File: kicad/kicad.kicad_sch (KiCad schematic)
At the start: 28 parts, among them J101 DEBUG_LED_CONN, J102 EPD_SPI_CONN, J103 HPC_CONN, J104 STORAGE_CONN, J105 MGMT_CONN, J106 GLOBAL_CONN, J107 INPUT_CONN, J109 USBC_CONN

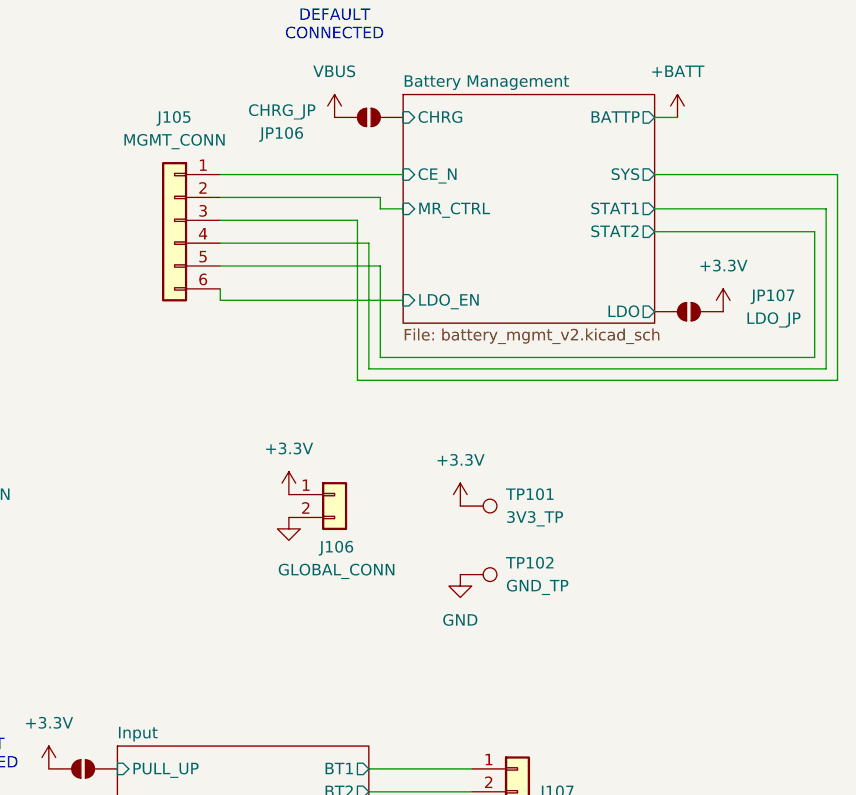
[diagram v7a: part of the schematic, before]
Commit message: slight refactoring, fix LDO power-path
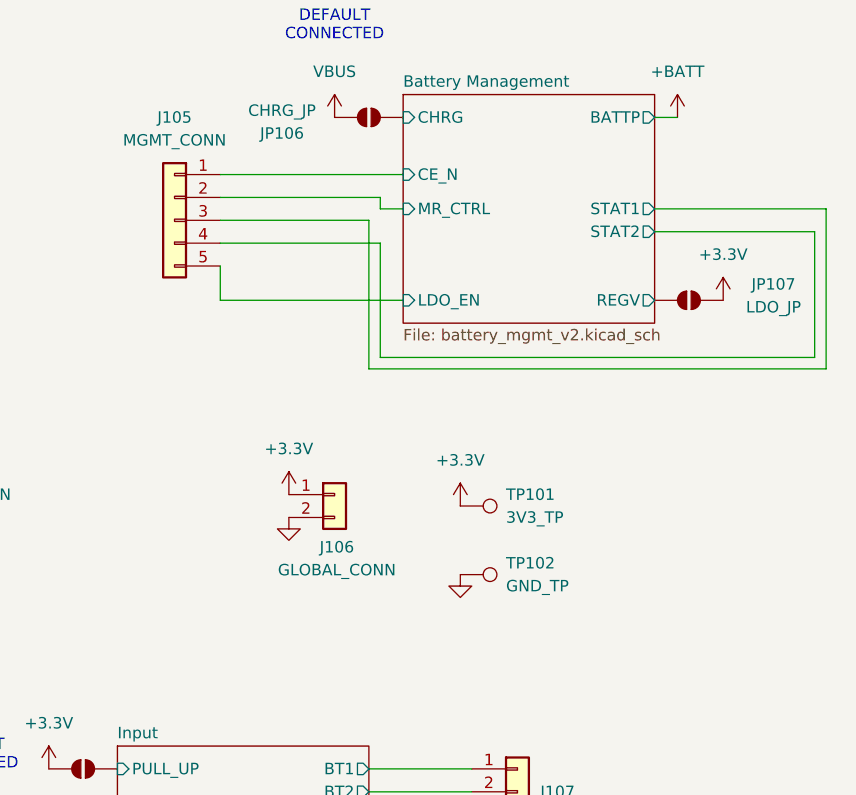
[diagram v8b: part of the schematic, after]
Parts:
- removed J105: MGMT_CONN, Connector_JST:JST_XH_B6B-XH-A_1x06_P2.50mm_Vertical, symbol Connector_Generic:Conn_01x06
- added J105: MGMT_CONN, symbol Connector_Generic:Conn_01x05
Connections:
- net Battery Management/CE_N: now also J105.1 (Pin_1)
- net Battery Management/LDO_EN: now also J105.5 (Pin_5)
- net Battery Management/MR_CTRL: now also J105.2 (Pin_2)
- net Battery Management/STAT1: now also J105.3 (Pin_3)
- net Battery Management/STAT2: now also J105.4 (Pin_4)
- net Battery Management/LDO renamed Battery Management/REGV
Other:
- sheet Battery Management ports: added REGV; removed LDO, SYS
- moved on the sheet: JP107
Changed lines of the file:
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@@
 	(wire
 		(pts
-			(xy 210.82 59.69) (xy 210.82 73.66)
+			(xy 210.82 57.15) (xy 210.82 73.66)
 		)
 		(stroke
@@
 	(wire
 		(pts
-			(xy 194.31 59.69) (xy 210.82 59.69)
+			(xy 210.82 118.11) (xy 222.25 118.11)
 		)
 		(stroke
@@
 	(wire
 		(pts
-			(xy 210.82 118.11) (xy 222.25 118.11)
+			(xy 260.35 72.39) (xy 260.35 58.42)
 		)
 		(stroke
@@
 	(wire
 		(pts
-			(xy 260.35 72.39) (xy 260.35 58.42)
+			(xy 38.1 138.43) (xy 67.31 138.43)
 		)
 		(stroke
@@
 	(wire
 		(pts
-			(xy 38.1 138.43) (xy 67.31 138.43)
+			(xy 194.31 57.15) (xy 210.82 57.15)
 		)
 		(stroke
@@
 	(wire
 		(pts
-			(xy 194.31 66.04) (xy 194.31 64.77)
-		)
-		(stroke
-			(width 0)
-			(type default)
-		)
-	)
-	(wire
-		(pts
-			(xy 209.55 74.93) (xy 262.89 74.93)
+			(xy 148.59 99.06) (xy 148.59 120.65)
 		)
 		(stroke
@@
 	(wire
 		(pts
-			(xy 148.59 99.06) (xy 148.59 120.65)
+			(xy 194.31 59.69) (xy 212.09 59.69)
 		)
 		(stroke
@@
 	(wire
 		(pts
-			(xy 209.55 57.15) (xy 209.55 74.93)
-		)
-		(stroke
-			(width 0)
-			(type default)
-		)
-	)
-	(wire
-		(pts
-			(xy 194.31 62.23) (xy 212.09 62.23)
-		)
-		(stroke
-			(width 0)
-			(type default)
-		)
-	)
-	(wire
-		(pts
 			(xy 151.13 119.38) (xy 151.13 101.6)
 		)
@@
 	(wire
 		(pts
-			(xy 262.89 52.07) (xy 242.57 52.07)
-		)
-		(stroke
-			(width 0)
-			(type default)
-		)
-	)
-	(wire
-		(pts
-			(xy 262.89 74.93) (xy 262.89 52.07)
+			(xy 194.31 52.07) (xy 214.63 52.07)
 		)
 		(stroke
@@
 	(wire
 		(pts
-			(xy 194.31 52.07) (xy 214.63 52.07)
+			(xy 110.49 167.64) (xy 124.46 167.64)
 		)
 		(stroke
@@
 	(wire
 		(pts
-			(xy 110.49 167.64) (xy 124.46 167.64)
+			(xy 210.82 123.19) (xy 222.25 123.19)
 		)
 		(stroke
@@
 	(wire
 		(pts
-			(xy 210.82 123.19) (xy 222.25 123.19)
+			(xy 123.19 162.56) (xy 110.49 162.56)
 		)
 		(stroke
@@
 	(wire
 		(pts
-			(xy 123.19 162.56) (xy 110.49 162.56)
+			(xy 194.31 62.23) (xy 194.31 66.04)
 		)
 		(stroke
@@
 	(wire
 		(pts
-			(xy 212.09 62.23) (xy 212.09 72.39)
-		)
-		(stroke
-			(width 0)
-			(type default)
-		)
-	)
-	(wire
-		(pts
-			(xy 214.63 66.04) (xy 194.31 66.04)
+			(xy 212.09 59.69) (xy 212.09 72.39)
 		)
 		(stroke
@@
 	(wire
 		(pts
-			(xy 194.31 57.15) (xy 209.55 57.15)
+			(xy 261.62 73.66) (xy 261.62 55.88)
 		)
 		(stroke
@@
 	(wire
 		(pts
-			(xy 261.62 73.66) (xy 261.62 55.88)
+			(xy 194.31 66.04) (xy 214.63 66.04)
 		)
 		(stroke
@@
 					(size 1.27 1.27)
 				)
+				(hide yes)
 			)
 		)
@@
 	)
 	(symbol
+		(lib_id "Connector_Generic:Conn_01x05")
+		(at 189.23 57.15 0)
+		(mirror y)
+		(unit 1)
+		(exclude_from_sim no)
+		(in_bom yes)
+		(on_board yes)
+		(dnp no)
+		(fields_autoplaced yes)
+		(property "Reference" "J105"
+			(at 189.23 45.72 0)
+			(effects
+				(font
+					(size 1.27 1.27)
+				)
+			)
+		)
+		(property "Value" "MGMT_CONN"
+			(at 189.23 48.26 0)
+			(effects
+				(font
+					(size 1.27 1.27)
+				)
+			)
+		)
+		(property "Footprint" ""
+			(at 189.23 57.15 0)
+			(effects
+				(font
+					(size 1.27 1.27)
+				)
+				(hide yes)
+			)
+		)
+		(property "Datasheet" "~"
+			(at 189.23 57.15 0)
+			(effects
+				(font
+					(size 1.27 1.27)
+				)
+				(hide yes)
+			)
+		)
+		(property "Description" "Generic connector, single row, 01x05, script generated (kicad-library-utils/schlib/autogen/connector/)"
+			(at 189.23 57.15 0)
+			(effects
+				(font
+					(size 1.27 1.27)
+				)
+				(hide yes)
+			)
+		)
+		(pin "5"
+		)
+		(pin "3"
+		)
+		(pin "1"
+		)
+		(pin "2"
+		)
+		(pin "4"
+		)
+		(instances
+			(project "kicad"
+				(path "/97e37379-fec6-4f0d-82d9-4ea53516bb02"
+					(reference "J105")
+					(unit 1)
+				)
+			)
+		)
+	)
+	(symbol
 		(lib_id "Device:R")
 		(at 63.5 104.14 0)
@@
 	)
 	(symbol
-		(lib_id "Connector_Generic:Conn_01x06")
-		(at 189.23 57.15 0)
-		(mirror y)
-		(unit 1)
-		(exclude_from_sim no)
-		(in_bom yes)
-		(on_board yes)
-		(dnp no)
-		(property "Reference" "J105"
-			(at 189.23 45.72 0)
-			(effects
-				(font
-					(size 1.27 1.27)
-				)
-			)
-		)
-		(property "Value" "MGMT_CONN"
-			(at 189.23 48.26 0)
-			(effects
-				(font
-					(size 1.27 1.27)
-				)
-			)
-		)
-		(property "Footprint" "Connector_JST:JST_XH_B6B-XH-A_1x06_P2.50mm_Vertical"
-			(at 189.23 57.15 0)
-			(effects
-				(font
-					(size 1.27 1.27)
-				)
-				(hide yes)
-			)
-		)
-		(property "Datasheet" "~"
-			(at 189.23 57.15 0)
-			(effects
-				(font
-					(size 1.27 1.27)
-				)
-				(hide yes)
-			)
-		)
-		(property "Description" "Generic connector, single row, 01x06, script generated (kicad-library-utils/schlib/autogen/connector/)"
-			(at 189.23 57.15 0)
-			(effects
-				(font
-					(size 1.27 1.27)
-				)
-				(hide yes)
-			)
-		)
-		(property "JLC" "XXXXXX"
-			(at 189.23 57.15 0)
-			(effects
-				(font
-					(size 1.27 1.27)
-				)
-				(hide yes)
-			)
-		)
-		(property "LCSC" "XXXXXX"
-			(at 189.23 57.15 0)
-			(effects
-				(font
-					(size 1.27 1.27)
-				)
-				(hide yes)
-			)
-		)
-		(pin "5"
-		)
-		(pin "2"
-		)
-		(pin "4"
-		)
-		(pin "6"
-		)
-		(pin "1"
-		)
-		(pin "3"
-		)
-		(instances
-			(project "kicad"
-				(path "/97e37379-fec6-4f0d-82d9-4ea53516bb02"
-					(reference "J105")
-					(unit 1)
-				)
-			)
-		)
-	)
-	(symbol
 		(lib_id "power:VBUS")
 		(at 149.86 45.72 0)
@@
 	(symbol
 		(lib_id "power:+3.3V")
-		(at 250.19 67.31 0)
+		(at 250.19 66.04 0)
 		(unit 1)
 		(exclude_from_sim no)
@@
 		(fields_autoplaced yes)
 		(property "Reference" "#PWR0122"
-			(at 250.19 71.12 0)
+			(at 250.19 69.85 0)
 			(effects
 				(font
@@
 		)
 		(property "Value" "+3.3V"
-			(at 250.19 62.23 0)
+			(at 250.19 60.96 0)
 			(effects
 				(font
@@
 		)
 		(property "Footprint" ""
-			(at 250.19 67.31 0)
+			(at 250.19 66.04 0)
 			(effects
 				(font
@@
 		)
 		(property "Datasheet" ""
-			(at 250.19 67.31 0)
+			(at 250.19 66.04 0)
 			(effects
 				(font
@@
 		)
 		(property "Description" "Power symbol creates a global label with name \"+3.3V\""
-			(at 250.19 67.31 0)
+			(at 250.19 66.04 0)
 			(effects
 				(font
@@
 	(symbol
 		(lib_id "Jumper:SolderJumper_2_Open")
-		(at 246.38 67.31 0)
+		(at 246.38 66.04 0)
 		(unit 1)
 		(exclude_from_sim yes)
@@
 		(dnp no)
 		(property "Reference" "JP107"
-			(at 255.778 65.532 0)
+			(at 255.778 64.262 0)
 			(effects
 				(font
@@
 		)
 		(property "Value" "LDO_JP"
-			(at 255.778 68.072 0)
+			(at 255.778 66.802 0)
 			(effects
 				(font
@@
 		)
 		(property "Footprint" "Jumper:SolderJumper-2_P1.3mm_Open_TrianglePad1.0x1.5mm"
-			(at 246.38 67.31 0)
+			(at 246.38 66.04 0)
 			(effects
 				(font
@@
 		)
 		(property "Datasheet" "~"
-			(at 246.38 67.31 0)
+			(at 246.38 66.04 0)
 			(effects
 				(font
@@
 		)
 		(property "Description" "Solder Jumper, 2-pole, open"
-			(at 246.38 67.31 0)
+			(at 246.38 66.04 0)
 			(effects
 				(font
@@
 		)
 		(property "JLC" "XXXXXX"
-			(at 246.38 67.31 0)
+			(at 246.38 66.04 0)
 			(effects
 				(font
@@
 		)
 		(property "LCSC" "XXXXXX"
-			(at 246.38 67.31 0)
+			(at 246.38 66.04 0)
 			(effects
 				(font
@@
 			)
 		)
-		(pin "LDO" output
-			(at 242.57 67.31 0)
-			(effects
-				(font
-					(size 1.27 1.27)
-				)
-				(justify right)
-			)
-		)
 		(pin "STAT2" output
 			(at 242.57 58.42 0)
@@
 			)
 		)
-		(pin "SYS" output
-			(at 242.57 52.07 0)
+		(pin "CE_N" input
+			(at 214.63 52.07 180)
 			(effects
 				(font
 					(size 1.27 1.27)
 				)
-				(justify right)
+				(justify left)
 			)
 		)
-		(pin "CE_N" input
-			(at 214.63 52.07 180)
+		(pin "REGV" output
+			(at 242.57 66.04 0)
 			(effects
 				(font
 					(size 1.27 1.27)
 				)
-				(justify left)
+				(justify right)
 			)
 		)
